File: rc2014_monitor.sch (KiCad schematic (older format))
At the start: 20 parts, among them J1 Z80 Bus, J2 Pro Bus, J3 USB_B_Micro, J4 Conn_01x01_Female, U3 74HCT244, U4 74HCT244, U5 74HCT244, U7 MAX40200AUK, U8 MAX40200AUK

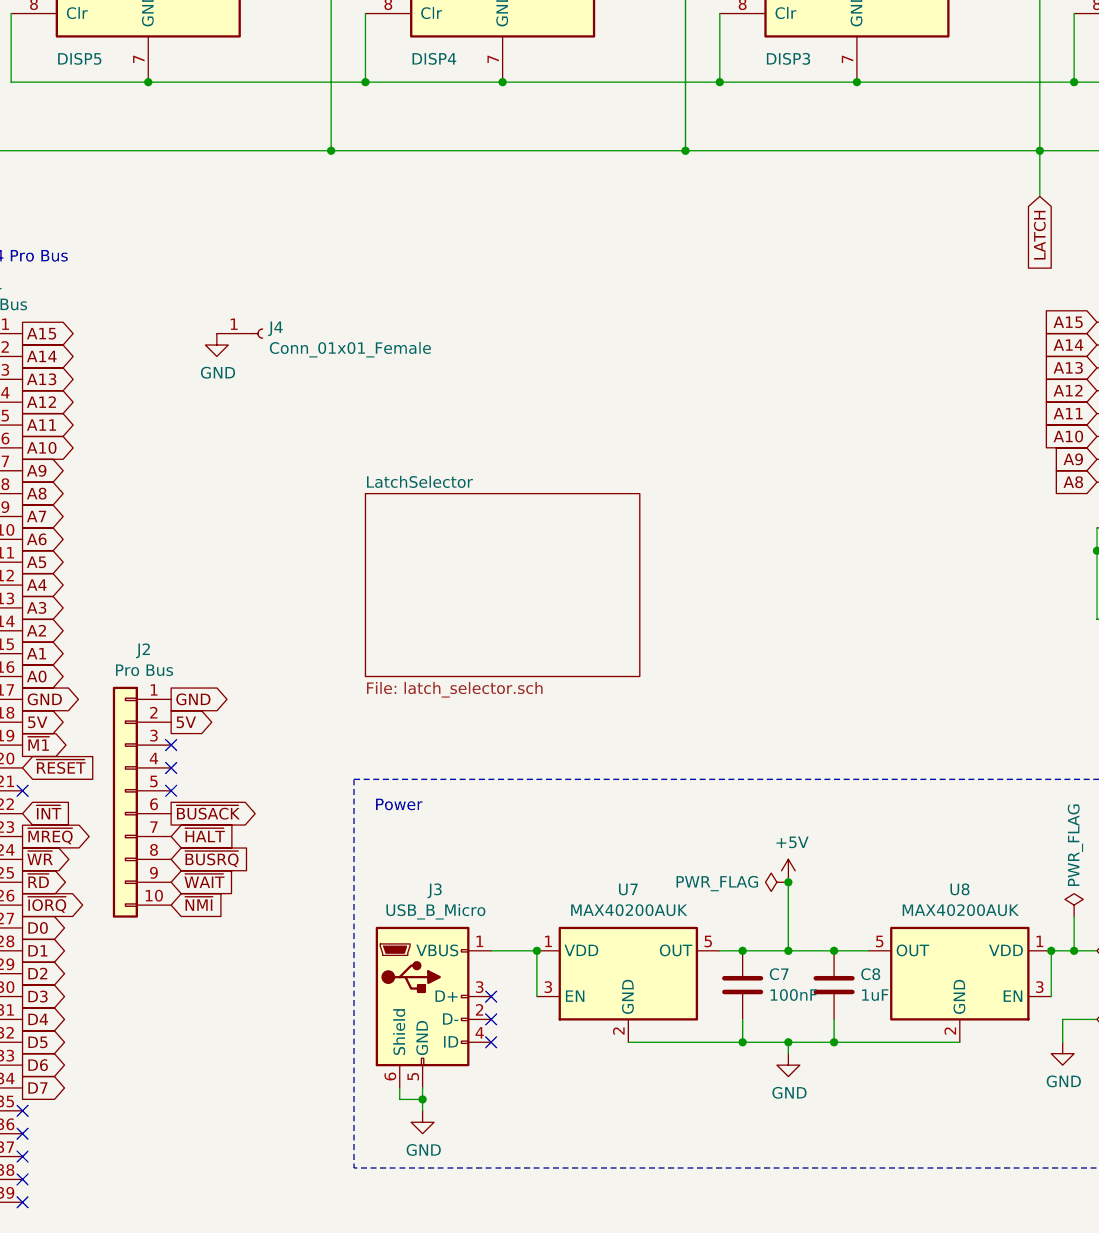
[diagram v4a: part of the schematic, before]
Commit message: Added reset circuit
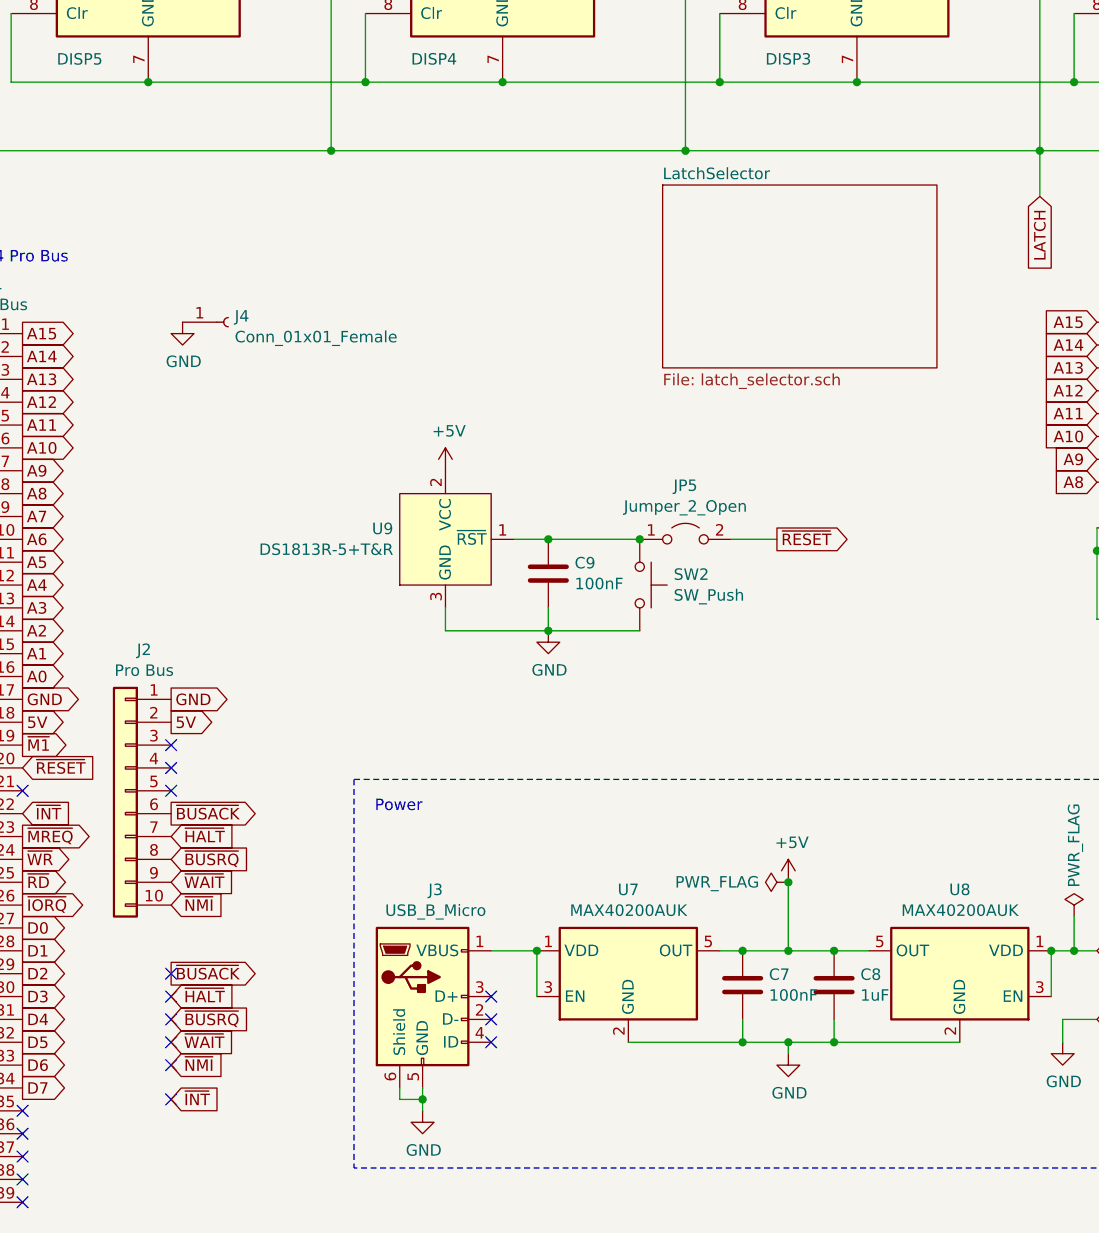
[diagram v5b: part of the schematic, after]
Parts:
- added C9: 100nF, Capacitor_SMD:C_0805_2012Metric_Pad1.15x1.40mm_HandSolder, symbol Device:C
- added JP5: Jumper_2_Open, Connector_PinHeader_2.54mm:PinHeader_1x02_P2.54mm_Vertical, symbol Jumper:Jumper_2_Open
- added SW2: SW_Push, Button_Switch_SMD:SW_SPST_EVQPE1, symbol Switch:SW_Push
- added U9: DS1813R-5+T&R, Package_TO_SOT_SMD:SOT-23, symbol Analog_Switch:DS1813R-5+T&R
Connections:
- net +5V: now also U9.2 (VCC)
- net GND: now also C9.2, SW2.2, U9.3 (GND)
- net ~RESET: now also JP5.2 (B)
- new net: C9.1, JP5.1 (A), SW2.1, U9.1 (~RST)
- no-connect marks 24 -> 30
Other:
- moved on the sheet: J4
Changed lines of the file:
@@
 	5950 6950 2450 6950
 $Sheet
-S 2500 4000 1200 800
+S 3800 2650 1200 800
 U 5CBDBC11
 F0 "LatchSelector" 50
@@
 L Connector:Conn_01x01_Female J4
 U 1 1 5CB841EA
-P 2050 3300
-F 0 "J4" H 2078 3326 50  0000 L CNN
-F 1 "Conn_01x01_Female" H 2078 3235 50  0000 L CNN
-F 2 "MountingHole:MountingHole_3.2mm_M3_ISO14580_Pad" H 2050 3300 50  0001 C CNN
-F 3 "~" H 2050 3300 50  0001 C CNN
-	1    2050 3300
+P 1900 3250
+F 0 "J4" H 1928 3276 50  0000 L CNN
+F 1 "Conn_01x01_Female" H 1928 3185 50  0000 L CNN
+F 2 "MountingHole:MountingHole_3.2mm_M3_ISO14580_Pad" H 1900 3250 50  0001 C CNN
+F 3 "~" H 1900 3250 50  0001 C CNN
+	1    1900 3250
 	1    0    0    -1
 $EndComp
@@
 L power:GND #PWR0119
 U 1 1 5CB8FB00
-P 1850 3300
+P 1700 3250
 AR Path="/5CB8FB00" Ref="#PWR0119"  Part="1"
 AR Path="/5CB63856/5CB8FB00" Ref="#PWR?"  Part="1"
 AR Path="/5CB5AB00/5CB63856/5CB8FB00" Ref="#PWR?"  Part="1"
-F 0 "#PWR0119" H 1850 3050 50  0001 C CNN
-F 1 "GND" H 1855 3127 50  0000 C CNN
-F 2 "" H 1850 3300 50  0001 C CNN
-F 3 "" H 1850 3300 50  0001 C CNN
-	1    1850 3300
+F 0 "#PWR0119" H 1700 3000 50  0001 C CNN
+F 1 "GND" H 1705 3077 50  0000 C CNN
+F 2 "" H 1700 3250 50  0001 C CNN
+F 3 "" H 1700 3250 50  0001 C CNN
+	1    1700 3250
 	1    0    0    -1
 $EndComp
@@
 Text GLabel 1000 5200 2    50   Input ~ 0
 ~RESET
+$Comp
+L Device:C C9
+U 1 1 5CB1BEC1
+P 3300 4350
+F 0 "C9" H 3415 4396 50  0000 L CNN
+F 1 "100nF" H 3415 4305 50  0000 L CNN
+F 2 "Capacitor_SMD:C_0805_2012Metric_Pad1.15x1.40mm_HandSolder" H 3338 4200 50  0001 C CNN
+F 3 "https://www.mouser.com/datasheet/2/427/Sprague%201C-3C%20MLC%20leaded%20capacitors%202000-1211470.pdf" H 3300 4350 50  0001 C CNN
+F 4 "Vishay" H -3350 -2350 50  0001 C CNN "MFR"
+F 5 "1C10Z5U104M050R" H -3350 -2350 50  0001 C CNN "MPN"
+F 6 "Mouser" H -3350 -2350 50  0001 C CNN "SPR"
+F 7 "75-1C10Z5U104M050R" H -3350 -2350 50  0001 C CNN "SPN"
+F 8 "-" H -3350 -2350 50  0001 C CNN "SPURL"
+	1    3300 4350
+	1    0    0    -1
+$EndComp
+Wire Wire Line
+	3150 4200 3300 4200
+$Comp
+L power:+5V #PWR0120
+U 1 1 5CB25D6C
+P 2850 3900
+AR Path="/5CB25D6C" Ref="#PWR0120"  Part="1"
+AR Path="/5CB63856/5CB25D6C" Ref="#PWR?"  Part="1"
+AR Path="/5CB5AB00/5CB63856/5CB25D6C" Ref="#PWR?"  Part="1"
+F 0 "#PWR0120" H 2850 3750 50  0001 C CNN
+F 1 "+5V" H 2865 4073 50  0000 C CNN
+F 2 "" H 2850 3900 50  0001 C CNN
+F 3 "" H 2850 3900 50  0001 C CNN
+	1    2850 3900
+	1    0    0    -1
+$EndComp
+$Comp
+L Switch:SW_Push SW2
+U 1 1 5CB2901B
+P 3700 4400
+F 0 "SW2" V 3654 4548 50  0000 L CNN
+F 1 "SW_Push" V 3745 4548 50  0000 L CNN
+F 2 "Button_Switch_SMD:SW_SPST_EVQPE1" H 3700 4600 50  0001 C CNN
+F 3 "~" H 3700 4600 50  0001 C CNN
+	1    3700 4400
+	0    1    1    0
+$EndComp
+Wire Wire Line
+	3700 4600 3300 4600
+Wire Wire Line
+	3300 4500 3300 4600
+Connection ~ 3300 4600
+Wire Wire Line
+	3700 4200 3300 4200
+Connection ~ 3300 4200
+Text GLabel 4300 4200 2    50   Output ~ 0
+~RESET
+Wire Wire Line
+	4300 4200 4100 4200
+$Comp
+L power:GND #PWR0121
+U 1 1 5CB41C00
+P 3300 4600
+AR Path="/5CB41C00" Ref="#PWR0121"  Part="1"
+AR Path="/5CB63856/5CB41C00" Ref="#PWR?"  Part="1"
+AR Path="/5CB5AB00/5CB63856/5CB41C00" Ref="#PWR?"  Part="1"
+F 0 "#PWR0121" H 3300 4350 50  0001 C CNN
+F 1 "GND" H 3305 4427 50  0000 C CNN
+F 2 "" H 3300 4600 50  0001 C CNN
+F 3 "" H 3300 4600 50  0001 C CNN
+	1    3300 4600
+	1    0    0    -1
+$EndComp
+$Comp
+L Jumper:Jumper_2_Open JP5
+U 1 1 5CB4C4BB
+P 3900 4200
+F 0 "JP5" H 3900 4435 50  0000 C CNN
+F 1 "Jumper_2_Open" H 3900 4344 50  0000 C CNN
+F 2 "Connector_PinHeader_2.54mm:PinHeader_1x02_P2.54mm_Vertical" H 3900 4200 50  0001 C CNN
+F 3 "~" H 3900 4200 50  0001 C CNN
+	1    3900 4200
+	1    0    0    -1
+$EndComp
+Connection ~ 3700 4200
+Wire Wire Line
+	2850 4500 2850 4600
+Wire Wire Line
+	2850 4600 3300 4600
+$Comp
+L Analog_Switch:DS1813R-5+T&R U9
+U 1 1 5CB1FDC4
+P 2850 4200
+F 0 "U9" H 2622 4246 50  0000 R CNN
+F 1 "DS1813R-5+T&R" H 2622 4155 50  0000 R CNN
+F 2 "Package_TO_SOT_SMD:SOT-23" H 2850 4700 50  0001 C CNN
+F 3 "https://www.mouser.com/datasheet/2/256/DS1233-1389125.pdf" H 2850 4700 50  0001 C CNN
+	1    2850 4200
+	1    0    0    -1
+$EndComp
+NoConn ~ 1650 6100
+NoConn ~ 1650 6200
+NoConn ~ 1650 6300
+NoConn ~ 1650 6400
+NoConn ~ 1650 6500
+NoConn ~ 1650 6650
+Text GLabel 1650 6650 2    50   Input ~ 0
+~INT
+Text GLabel 1650 6100 2    50   Output ~ 0
+~BUSACK
+Text GLabel 1650 6200 2    50   Input ~ 0
+~HALT
+Text GLabel 1650 6300 2    50   Input ~ 0
+~BUSRQ
+Text GLabel 1650 6400 2    50   Input ~ 0
+~WAIT
+Text GLabel 1650 6500 2    50   Input ~ 0
+~NMI
 $EndSCHEMATC

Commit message: label updates
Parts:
- J4: value Conn_01x01_Female -> M3 Mounting Hole
- JP5: value Jumper_2_Open -> Reset Enable
- U9: symbol Analog_Switch:DS1813R-5+T&R -> rc2014_monitor-rescue:DS1813R-5+T&R-Analog_Switch
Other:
- note added: "Reset Monitor"
- moved on the sheet: C3, C4, C5, C7, C8, C9, DISP0, DISP1, DISP2, DISP3, DISP4, DISP5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

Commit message: Changed display buffer and other parts
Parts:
- removed U3, U4, U5: 74HCT244, Package_DIP:DIP-20_W7.62mm_Socket, symbol 74xx:74HCT244
- added U3, U4, U5: 74HCT541, Package_DIP:DIP-20_W7.62mm, symbol 74xx:74HCT541
- C3, C4, C5: footprint Capacitor_THT:C_Disc_D5.0mm_W2.5mm_P2.50mm -> Capacitor_SMD:C_0805_2012Metric_Pad1.15x1.40mm_HandSolder; MFR Vishay -> KEMET; MPN 1C10Z5U104M050R -> C0805C104K4RACTU; SPN 75-1C10Z5U104M050R -> 80-C0805C104K4R; SPURL - -> https://www.mouser.com/ProductDetail/KEMET/C0805C104K4RACTU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
- C7, C9: MFR Vishay -> KEMET; MPN 1C10Z5U104M050R -> C0805C104K4RACTU; SPN 75-1C10Z5U104M050R -> 80-C0805C104K4R; SPURL - -> https://www.mouser.com/ProductDetail/KEMET/C0805C104K4RACTU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
- C8: MFR Vishay -> KEMET; MPN 1C10Z5U104M050R -> C0805C105K4RACTU; SPN 75-1C10Z5U104M050R -> 80-C0805C105K4R; SPURL - -> https://www.mouser.com/ProductDetail/KEMET/C0805C105K8RAC72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
- J3: SPURL - -> https://www.mouser.com/ProductDetail/Amphenol-FCI/10103594-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
- SW2: MFR (none) -> Panasonic; MPN (none) -> EVQ-PE105K; SPN (none) -> 667-EVQ-PE105K; SPR (none) -> Mouser; SPURL (none) -> https://www.mouser.com/ProductDetail/Panasonic/EVQ-PE105K?q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
- U7, U8: footprint Package_TO_SOT_SMD:SOT-23-5 -> Package_TO_SOT_SMD:SOT-23-5_HandSoldering
- U9: MFR (none) -> Maxim Integrated; MPN (none) -> DS1813R-5+T&R; SPN (none) -> 700-DS1813R-5T&R; SPR (none) -> Mouser; SPURL (none) -> https://www.mouser.com/ProductDetail/Maxim-Integrated/DS181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
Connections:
- net +5V: now also U3.20 (VCC), U4.20 (VCC), U5.20 (VCC)
- net A0: now also U4.9 (A7)
- net A1: now also U4.8 (A6)
- net A10: now also U3.7 (A5)
- net A11: now also U3.6 (A4)
- net A12: now also U3.5 (A3)
- net A13: now also U3.4 (A2)
- net A14: now also U3.3 (A1)
- net A15: now also U3.2 (A0)
- net A2: now also U4.7 (A5)
- net A3: now also U4.6 (A4)
- net A4: now also U4.5 (A3)
- net A5: now also U4.4 (A2)
- net A6: now also U4.3 (A1)
- net A7: now also U4.2 (A0)
- net A8: now also U3.9 (A7)
- net A9: now also U3.8 (A6)
- net D0: now also U5.2 (A0)
- net D1: now also U5.3 (A1)
- net D2: now also U5.4 (A2)
- net D3: now also U5.5 (A3)
- net D4: now also U5.6 (A4)
- net D5: now also U5.7 (A5)
- net D6: now also U5.8 (A6)
- net D7: now also U5.9 (A7)
- net D_A0: now also U4.11 (Y7)
- net D_A1: now also U4.12 (Y6)
- net D_A10: now also U3.13 (Y5)
- net D_A11: now also U3.14 (Y4)
- net D_A12: now also U3.15 (Y3)
- net D_A13: now also U3.16 (Y2)
- net D_A14: now also U3.17 (Y1)
- net D_A15: now also U3.18 (Y0)
- net D_A2: now also U4.13 (Y5)
- net D_A3: now also U4.14 (Y4)
- net D_A4: now also U4.15 (Y3)
- net D_A5: now also U4.16 (Y2)
- net D_A6: now also U4.17 (Y1)
- net D_A7: now also U4.18 (Y0)
- net D_A8: now also U3.11 (Y7)
- net D_A9: now also U3.12 (Y6)
- net D_D0: now also U5.18 (Y0)
- net D_D1: now also U5.17 (Y1)
- net D_D2: now also U5.16 (Y2)
- net D_D3: now also U5.15 (Y3)
- net D_D4: now also U5.14 (Y4)
- net D_D5: now also U5.13 (Y5)
- net D_D6: now also U5.12 (Y6)
- net D_D7: now also U5.11 (Y7)
- net GND: now also U3.1 (G1), U3.10 (GND), U3.19 (G2), U4.1 (G1), U4.10 (GND), U4.19 (G2), U5.1 (G1), U5.10 (GND), U5.19 (G2)
- no-connect marks 30 -> 29

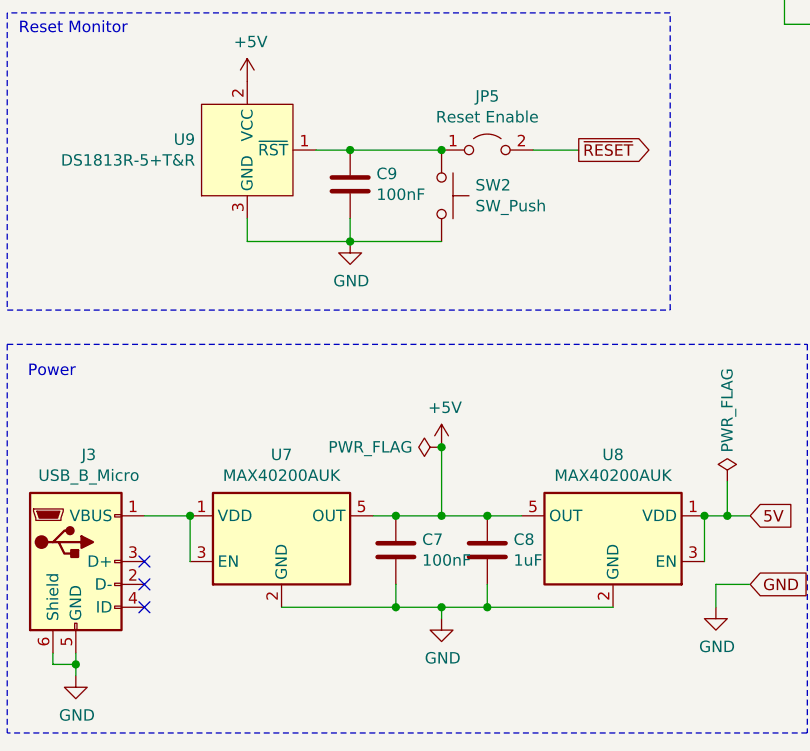
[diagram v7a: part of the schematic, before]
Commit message: labelling and layout fixes
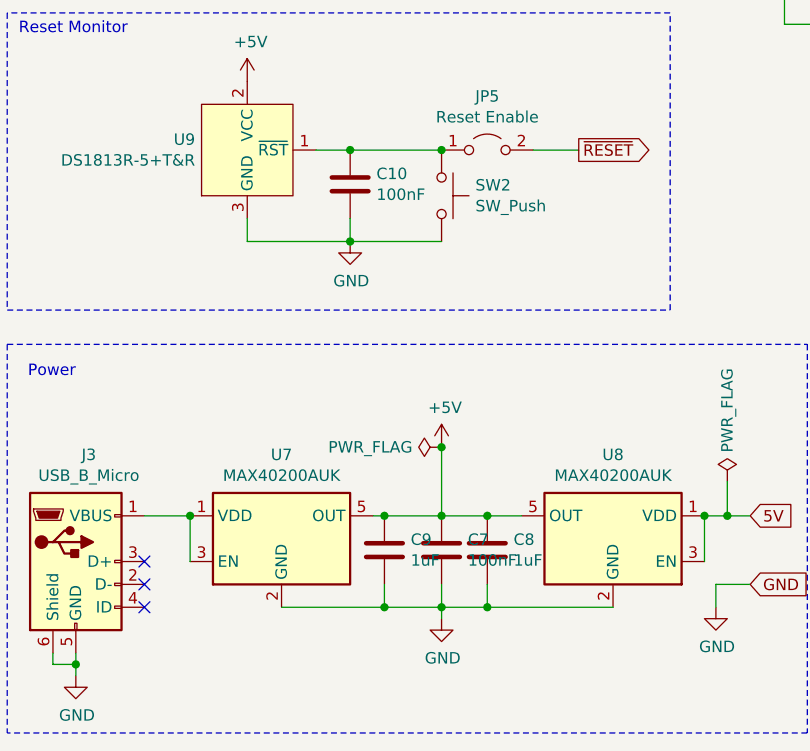
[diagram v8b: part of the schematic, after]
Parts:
- added C9: 1uF, Capacitor_SMD:C_0805_2012Metric_Pad1.15x1.40mm_HandSolder, symbol Device:C
- SW2: footprint Button_Switch_SMD:SW_SPST_EVQPE1 -> Button_Switch_THT:SW_PUSH_6mm
- renumbered C9 to C10
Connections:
- net +5V: now also C9.1
- net GND: now also C9.2
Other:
- moved on the sheet: C7
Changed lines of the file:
@@
 L Device:C C7
 U 1 1 5CB2CAB8
-P 4050 6850
-F 0 "C7" H 4165 6896 50  0000 L CNN
-F 1 "100nF" H 4165 6805 50  0000 L CNN
-F 2 "Capacitor_SMD:C_0805_2012Metric_Pad1.15x1.40mm_HandSolder" H 4088 6700 50  0001 C CNN
-F 3 "https://www.mouser.com/datasheet/2/212/KEM_C1002_X7R_SMD-1102033.pdf" H 4050 6850 50  0001 C CNN
-F 4 "KEMET" H -2600 150 50  0001 C CNN "MFR"
-F 5 "C0805C104K4RACTU" H -2600 150 50  0001 C CNN "MPN"
-F 6 "Mouser" H -2600 150 50  0001 C CNN "SPR"
-F 7 "80-C0805C104K4R" H -2600 150 50  0001 C CNN "SPN"
-F 8 "https://www.mouser.com/ProductDetail/KEMET/C0805C104K4RACTU?qs=sGAEpiMZZMs0AnBnWHyRQFCCI5cSbRT%2F1Gdrl2EbPVM%3D" H -2600 150 50  0001 C CNN "SPURL"
-	1    4050 6850
+P 4250 6850
+F 0 "C7" H 4365 6896 50  0000 L CNN
+F 1 "100nF" H 4365 6805 50  0000 L CNN
+F 2 "Capacitor_SMD:C_0805_2012Metric_Pad1.15x1.40mm_HandSolder" H 4288 6700 50  0001 C CNN
+F 3 "https://www.mouser.com/datasheet/2/212/KEM_C1002_X7R_SMD-1102033.pdf" H 4250 6850 50  0001 C CNN
+F 4 "KEMET" H -2400 150 50  0001 C CNN "MFR"
+F 5 "C0805C104K4RACTU" H -2400 150 50  0001 C CNN "MPN"
+F 6 "Mouser" H -2400 150 50  0001 C CNN "SPR"
+F 7 "80-C0805C104K4R" H -2400 150 50  0001 C CNN "SPN"
+F 8 "https://www.mouser.com/ProductDetail/KEMET/C0805C104K4RACTU?qs=sGAEpiMZZMs0AnBnWHyRQFCCI5cSbRT%2F1Gdrl2EbPVM%3D" H -2400 150 50  0001 C CNN "SPURL"
+	1    4250 6850
 	1    0    0    -1
 $EndComp
@@
 Connection ~ 3150 6700
 Wire Wire Line
-	4050 6700 4250 6700
-Wire Wire Line
-	3550 7100 4050 7100
-Wire Wire Line
-	4050 7000 4050 7100
-Connection ~ 4050 7100
-Wire Wire Line
-	4050 7100 4250 7100
-Wire Wire Line
-	3950 6700 4050 6700
-Connection ~ 4050 6700
+	4250 7000 4250 7100
 Wire Wire Line
 	5450 7000 5450 7100
@@
 ~RESET
 $Comp
-L Device:C C9
+L Device:C C10
 U 1 1 5CB1BEC1
 P 3850 5250
-F 0 "C9" H 3965 5296 50  0000 L CNN
+F 0 "C10" H 3965 5296 50  0000 L CNN
 F 1 "100nF" H 3965 5205 50  0000 L CNN
 F 2 "Capacitor_SMD:C_0805_2012Metric_Pad1.15x1.40mm_HandSolder" H 3888 5100 50  0001 C CNN
@@
 F 0 "SW2" V 4204 5448 50  0000 L CNN
 F 1 "SW_Push" V 4295 5448 50  0000 L CNN
-F 2 "Button_Switch_SMD:SW_SPST_EVQPE1" H 4250 5500 50  0001 C CNN
+F 2 "Button_Switch_THT:SW_PUSH_6mm" H 4250 5500 50  0001 C CNN
 F 3 "https://www.mouser.com/datasheet/2/315/sw_lt_eng_6035s-1289049.pdf" H 4250 5500 50  0001 C CNN
 F 4 "Panasonic" H 0   0   50  0001 C CNN "MFR"
@@
 	7650 4250 7650 4150
 Connection ~ 7650 4250
+Wire Wire Line
+	3950 6700 4000 6700
+Wire Wire Line
+	3550 7100 4000 7100
+$Comp
+L Device:C C9
+U 1 1 5CCF3BD8
+P 4000 6850
+F 0 "C9" H 4115 6896 50  0000 L CNN
+F 1 "1uF" H 4115 6805 50  0000 L CNN
+F 2 "Capacitor_SMD:C_0805_2012Metric_Pad1.15x1.40mm_HandSolder" H 4038 6700 50  0001 C CNN
+F 3 "https://www.mouser.com/datasheet/2/212/KEM_C1002_X7R_SMD-1102033.pdf" H 4000 6850 50  0001 C CNN
+F 4 "KEMET" H -2650 150 50  0001 C CNN "MFR"
+F 5 "C0805C105K4RACTU" H -2650 150 50  0001 C CNN "MPN"
+F 6 "Mouser" H -2650 150 50  0001 C CNN "SPR"
+F 7 "80-C0805C105K4R" H -2650 150 50  0001 C CNN "SPN"
+F 8 "https://www.mouser.com/ProductDetail/KEMET/C0805C105K8RAC7210?qs=sGAEpiMZZMs0AnBnWHyRQOf5HOpVaXbh6p7WVhSDTqQ%3D" H -2650 150 50  0001 C CNN "SPURL"
+	1    4000 6850
+	1    0    0    -1
+$EndComp
+Connection ~ 4000 6700
+Wire Wire Line
+	4000 6700 4250 6700
+Wire Wire Line
+	4000 7000 4000 7100
+Connection ~ 4000 7100
+Wire Wire Line
+	4000 7100 4250 7100
 $EndSCHEMATC
